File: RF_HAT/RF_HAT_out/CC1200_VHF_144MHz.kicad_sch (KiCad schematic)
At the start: 42 parts, among them J2 SMA, U2 CC1200RHBR, Y2 40MHz

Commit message: switch to SMD pico
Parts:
- TP5, TP6, TP7, TP8: value (none) -> ~

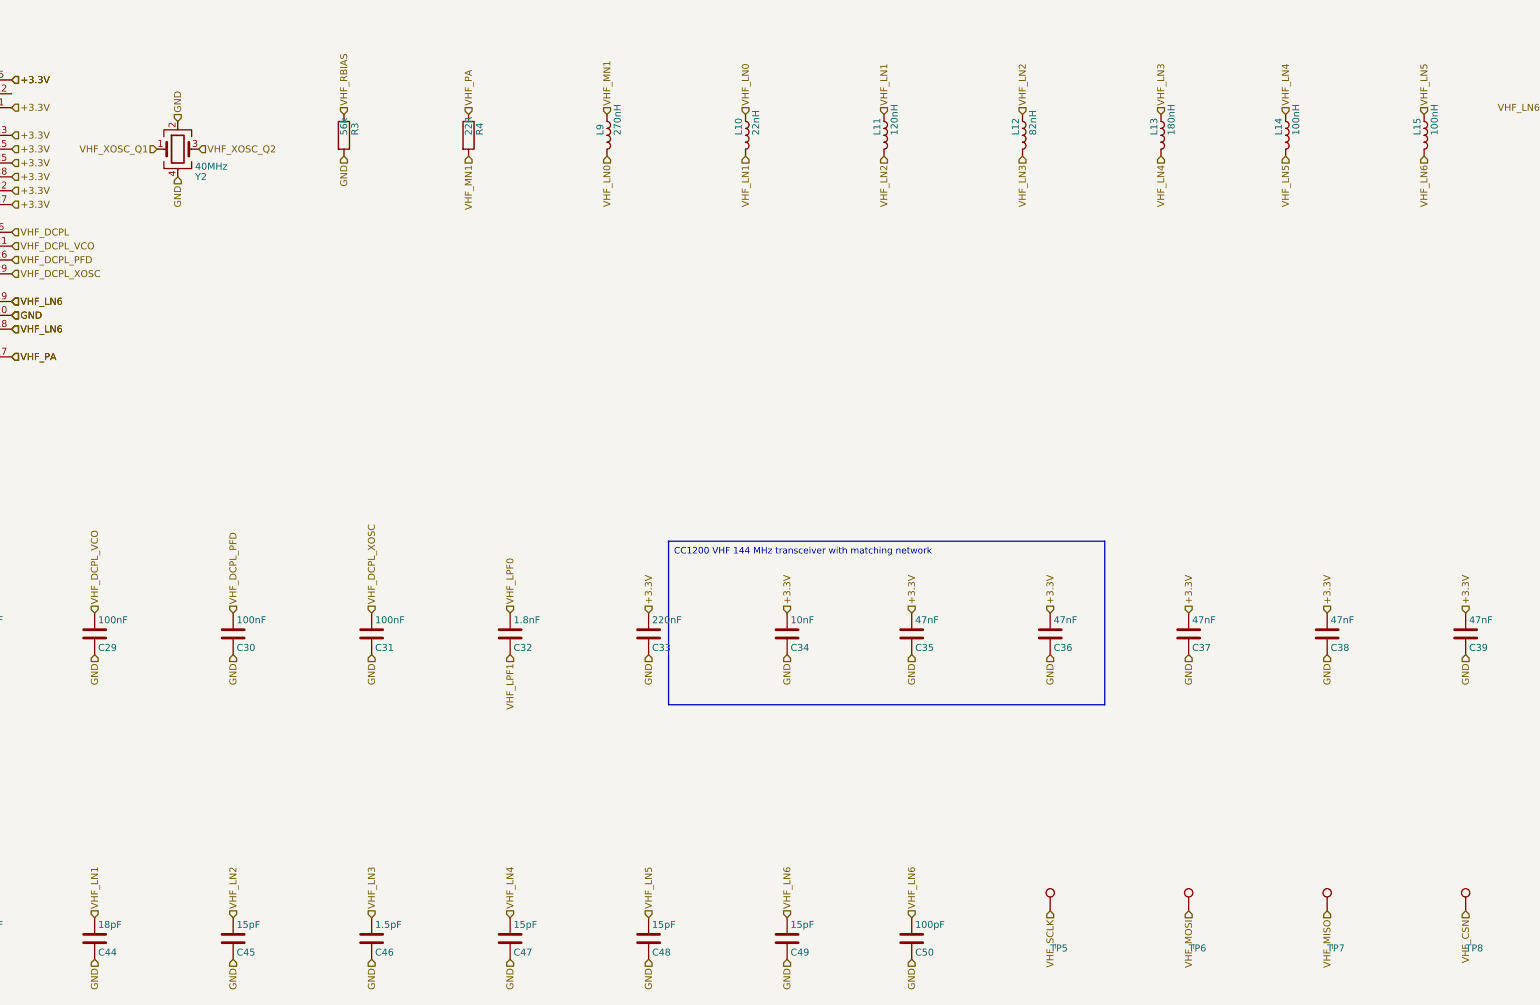
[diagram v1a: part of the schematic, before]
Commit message: switched to 0603 for all passives
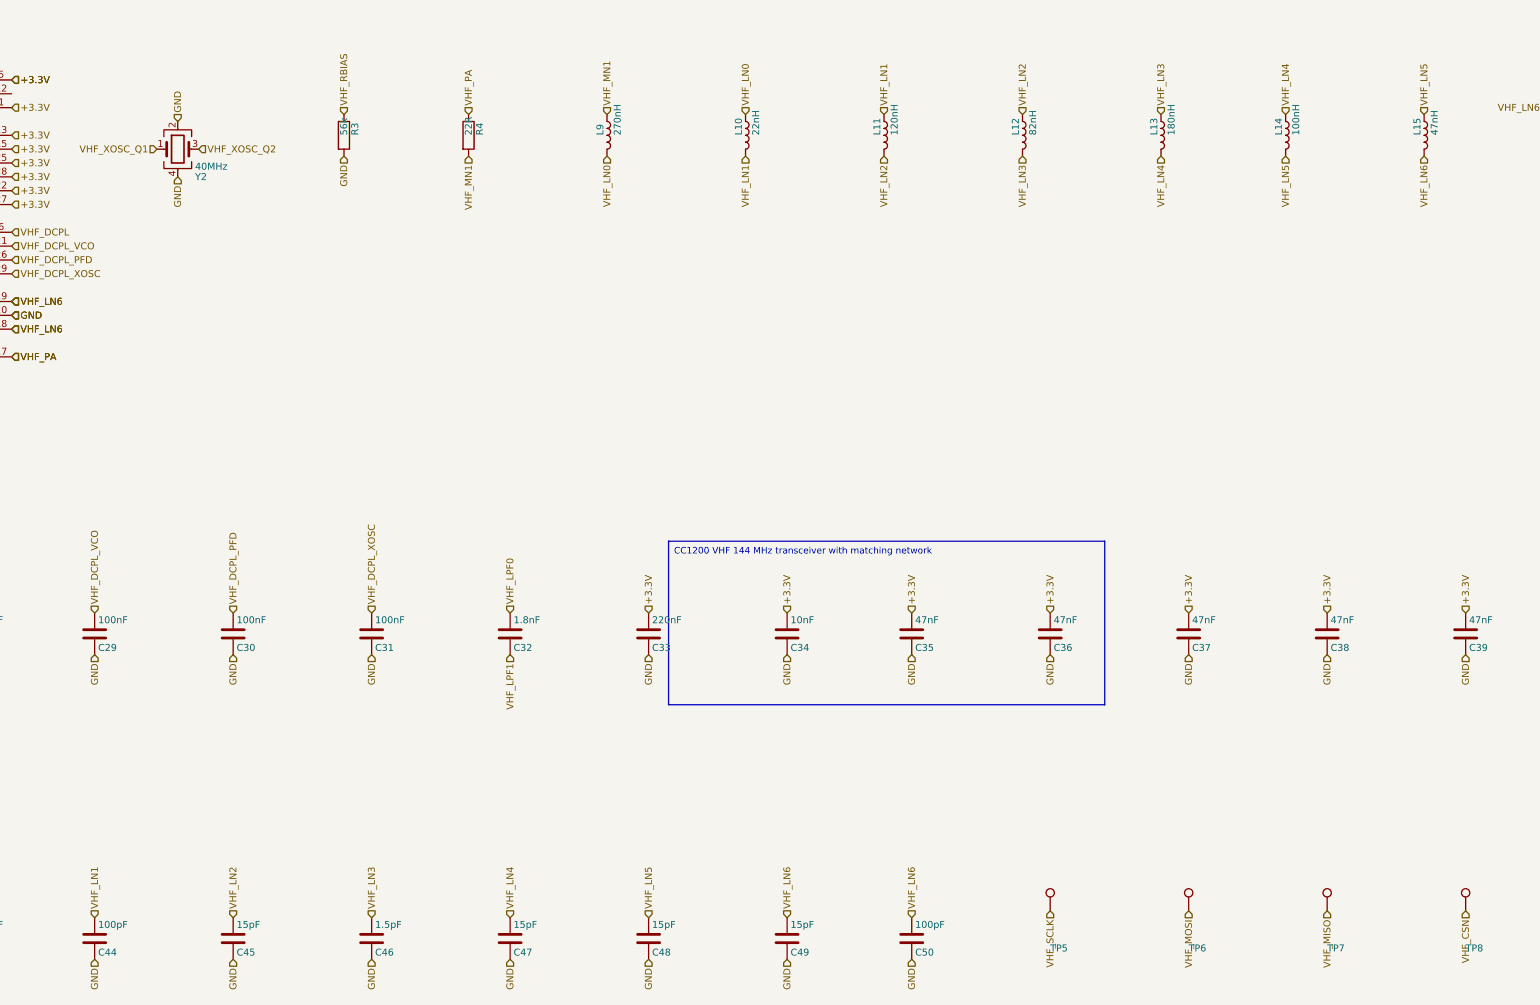
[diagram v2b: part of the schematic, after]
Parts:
- C26, C27: footprint Capacitor_SMD:C_0805_2012Metric -> Capacitor_SMD:C_0603_1608Metric; hierarchy_path /03cc9bb1-75ec-4755-9977-259c49401791/b9885f1a-c8d9-48d7-b8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 -> /bd07fb41-9ea7-4d0f-b403-cbcdc979b1cd/be5c3a7c-20a8-4363-bf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; root_uuid 03cc9bb1-75ec-4755-9977-259c49401791 -> bd07fb41-9ea7-4d0f-b403-cbcdc979b1cd
- C28, C29, C30, C31, C32, C33, C34, C35, C36, C37, C38, C39, C40, C41, C42: footprint Capacitor_SMD:C_0402_1005Metric -> Capacitor_SMD:C_0603_1608Metric; hierarchy_path /03cc9bb1-75ec-4755-9977-259c49401791/b9885f1a-c8d9-48d7-b8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 -> /bd07fb41-9ea7-4d0f-b403-cbcdc979b1cd/be5c3a7c-20a8-4363-bf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; root_uuid 03cc9bb1-75ec-4755-9977-259c49401791 -> bd07fb41-9ea7-4d0f-b403-cbcdc979b1cd
- C43, C45, C46, C47, C48, C49, C50, J2, L10, L11, L12, L13, L14, L9, TP5, TP6, TP7, TP8, U2, Y2: hierarchy_path /03cc9bb1-75ec-4755-9977-259c49401791/b9885f1a-c8d9-48d7-b8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 -> /bd07fb41-9ea7-4d0f-b403-cbcdc979b1cd/be5c3a7c-20a8-4363-bf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; root_uuid 03cc9bb1-75ec-4755-9977-259c49401791 -> bd07fb41-9ea7-4d0f-b403-cbcdc979b1cd
- C44: value 18pF -> 100pF; hierarchy_path /03cc9bb1-75ec-4755-9977-259c49401791/b9885f1a-c8d9-48d7-b8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 -> /bd07fb41-9ea7-4d0f-b403-cbcdc979b1cd/be5c3a7c-20a8-4363-bf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; root_uuid 03cc9bb1-75ec-4755-9977-259c49401791 -> bd07fb41-9ea7-4d0f-b403-cbcdc979b1cd
- FB2: footprint Inductor_SMD:L_0402_1005Metric -> Inductor_SMD:L_0603_1608Metric; hierarchy_path /03cc9bb1-75ec-4755-9977-259c49401791/b9885f1a-c8d9-48d7-b8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 -> /bd07fb41-9ea7-4d0f-b403-cbcdc979b1cd/be5c3a7c-20a8-4363-bf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; root_uuid 03cc9bb1-75ec-4755-9977-259c49401791 -> bd07fb41-9ea7-4d0f-b403-cbcdc979b1cd
- L15: value 100nH -> 47nH; hierarchy_path /03cc9bb1-75ec-4755-9977-259c49401791/b9885f1a-c8d9-48d7-b8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 -> /bd07fb41-9ea7-4d0f-b403-cbcdc979b1cd/be5c3a7c-20a8-4363-bf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; root_uuid 03cc9bb1-75ec-4755-9977-259c49401791 -> bd07fb41-9ea7-4d0f-b403-cbcdc979b1cd
- R3: footprint Resistor_SMD:R_0402_1005Metric -> Resistor_SMD:R_0603_1608Metric; hierarchy_path /03cc9bb1-75ec-4755-9977-259c49401791/b9885f1a-c8d9-48d7-b8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 -> /bd07fb41-9ea7-4d0f-b403-cbcdc979b1cd/be5c3a7c-20a8-4363-bf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; root_uuid 03cc9bb1-75ec-4755-9977-259c49401791 -> bd07fb41-9ea7-4d0f-b403-cbcdc979b1cd
- R4: footprint Resistor_SMD:R_0805_2012Metric -> Resistor_SMD:R_0603_1608Metric; hierarchy_path /03cc9bb1-75ec-4755-9977-259c49401791/b9885f1a-c8d9-48d7-b8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 -> /bd07fb41-9ea7-4d0f-b403-cbcdc979b1cd/be5c3a7c-20a8-4363-bf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; root_uuid 03cc9bb1-75ec-4755-9977-259c49401791 -> bd07fb41-9ea7-4d0f-b403-cbcdc979b1cd

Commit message: first routing of signals
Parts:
- removed TP5, TP6, TP7, TP8: ~, TestPoint:TestPoint_Pad_D1.0mm, symbol Connector:TestPoint
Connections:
- net +3.3V: no longer C33.1, C34.1, C35.1, C36.1, C37.1, C38.1, C39.1, C40.1, C41.1, U2.1 (VDD_GUARD), U2.13 (AVDD_IF), U2.15 (AVDD_RF), U2.22 (AVDD_SYNTH1), U2.25 (AVDD_PFD_CHP), U2.27 (AVDD_SYNTH2), U2.28 (AVDD_XOSC), U2.5 (DVDD)
- net VHF_AVDD_FILT: now also C33.1, C34.1, C35.1, C36.1, C37.1, C38.1, C39.1, C40.1, C41.1, U2.1 (VDD_GUARD), U2.12 (DVDD), U2.13 (AVDD_IF), U2.15 (AVDD_RF), U2.22 (AVDD_SYNTH1), U2.25 (AVDD_PFD_CHP), U2.27 (AVDD_SYNTH2), U2.28 (AVDD_XOSC), U2.5 (DVDD)

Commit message: Restructured kicad schematic for CC1200 PI_HAT readablitity based on M17 reference schematics
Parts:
- removed C48, C49: 15pF, Capacitor_SMD:C_0603_1608Metric, symbol Device:C
- removed C50: 100pF, Capacitor_SMD:C_0603_1608Metric, symbol Device:C
- removed FB2: 1k@100MHz, Inductor_SMD:L_0603_1608Metric, symbol Device:FerriteBead
- removed R4: 22R, Resistor_SMD:R_0603_1608Metric, symbol Device:R
- added C11, C20: 15pF, Capacitor_SMD:C_0603_1608Metric, symbol Device:C
- added C23: 1.8nF, Capacitor_SMD:C_0603_1608Metric, symbol Device:C
- added C25: 47nF, Capacitor_SMD:C_0603_1608Metric, symbol Device:C
- added L16: 82nH, Inductor_SMD:L_0603_1608Metric, symbol Device:L
- added R1, R2: 10k, Resistor_SMD:R_0603_1608Metric, symbol Device:R
- added R8: 22R, Resistor_SMD:R_0603_1608Metric, symbol Device:R
- C26: value 15pF -> 47nF; hierarchy_path /bd07fb41-9ea7-4d0f-b403-cbcdc979b1cd/be5c3a7c-20a8-4363-bf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 -> /300cf3d4-e317-44c8-acd8-5f9989779c7c/4304a2bc-ba15-4549-9a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; root_uuid bd07fb41-9ea7-4d0f-b403-cbcdc979b1cd -> 300cf3d4-e317-44c8-acd8-5f9989779c7c
- C27, C35, C36, C37, C40, C43, C45, J2, R3, U2, Y2: hierarchy_path /bd07fb41-9ea7-4d0f-b403-cbcdc979b1cd/be5c3a7c-20a8-4363-bf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 -> /300cf3d4-e317-44c8-acd8-5f9989779c7c/4304a2bc-ba15-4549-9a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; root_uuid bd07fb41-9ea7-4d0f-b403-cbcdc979b1cd -> 300cf3d4-e317-44c8-acd8-5f9989779c7c
- C28, C29, C30: value 100nF -> 47nF; hierarchy_path /bd07fb41-9ea7-4d0f-b403-cbcdc979b1cd/be5c3a7c-20a8-4363-bf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 -> /300cf3d4-e317-44c8-acd8-5f9989779c7c/4304a2bc-ba15-4549-9a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; root_uuid bd07fb41-9ea7-4d0f-b403-cbcdc979b1cd -> 300cf3d4-e317-44c8-acd8-5f9989779c7c
- C31: value 100nF -> 10nF; hierarchy_path /bd07fb41-9ea7-4d0f-b403-cbcdc979b1cd/be5c3a7c-20a8-4363-bf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 -> /300cf3d4-e317-44c8-acd8-5f9989779c7c/4304a2bc-ba15-4549-9a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; root_uuid bd07fb41-9ea7-4d0f-b403-cbcdc979b1cd -> 300cf3d4-e317-44c8-acd8-5f9989779c7c
- C32: value 1.8nF -> 15pF; hierarchy_path /bd07fb41-9ea7-4d0f-b403-cbcdc979b1cd/be5c3a7c-20a8-4363-bf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 -> /300cf3d4-e317-44c8-acd8-5f9989779c7c/4304a2bc-ba15-4549-9a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; root_uuid bd07fb41-9ea7-4d0f-b403-cbcdc979b1cd -> 300cf3d4-e317-44c8-acd8-5f9989779c7c
- C33: value 220nF -> 47nF; hierarchy_path /bd07fb41-9ea7-4d0f-b403-cbcdc979b1cd/be5c3a7c-20a8-4363-bf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 -> /300cf3d4-e317-44c8-acd8-5f9989779c7c/4304a2bc-ba15-4549-9a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; root_uuid bd07fb41-9ea7-4d0f-b403-cbcdc979b1cd -> 300cf3d4-e317-44c8-acd8-5f9989779c7c
- C34: value 10nF -> 220nF; hierarchy_path /bd07fb41-9ea7-4d0f-b403-cbcdc979b1cd/be5c3a7c-20a8-4363-bf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 -> /300cf3d4-e317-44c8-acd8-5f9989779c7c/4304a2bc-ba15-4549-9a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; root_uuid bd07fb41-9ea7-4d0f-b403-cbcdc979b1cd -> 300cf3d4-e317-44c8-acd8-5f9989779c7c
- C38, C39: value 47nF -> 100pF; hierarchy_path /bd07fb41-9ea7-4d0f-b403-cbcdc979b1cd/be5c3a7c-20a8-4363-bf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 -> /300cf3d4-e317-44c8-acd8-5f9989779c7c/4304a2bc-ba15-4549-9a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; root_uuid bd07fb41-9ea7-4d0f-b403-cbcdc979b1cd -> 300cf3d4-e317-44c8-acd8-5f9989779c7c
- C41: value 47nF -> 10nF; hierarchy_path /bd07fb41-9ea7-4d0f-b403-cbcdc979b1cd/be5c3a7c-20a8-4363-bf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 -> /300cf3d4-e317-44c8-acd8-5f9989779c7c/4304a2bc-ba15-4549-9a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; root_uuid bd07fb41-9ea7-4d0f-b403-cbcdc979b1cd -> 300cf3d4-e317-44c8-acd8-5f9989779c7c
- C42: value 10nF -> 47nF; hierarchy_path /bd07fb41-9ea7-4d0f-b403-cbcdc979b1cd/be5c3a7c-20a8-4363-bf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 -> /300cf3d4-e317-44c8-acd8-5f9989779c7c/4304a2bc-ba15-4549-9a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; root_uuid bd07fb41-9ea7-4d0f-b403-cbcdc979b1cd -> 300cf3d4-e317-44c8-acd8-5f9989779c7c
- C44: value 100pF -> 1.5pF; hierarchy_path /bd07fb41-9ea7-4d0f-b403-cbcdc979b1cd/be5c3a7c-20a8-4363-bf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 -> /300cf3d4-e317-44c8-acd8-5f9989779c7c/4304a2bc-ba15-4549-9a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; root_uuid bd07fb41-9ea7-4d0f-b403-cbcdc979b1cd -> 300cf3d4-e317-44c8-acd8-5f9989779c7c
- C46: value 1.5pF -> 15pF; hierarchy_path /bd07fb41-9ea7-4d0f-b403-cbcdc979b1cd/be5c3a7c-20a8-4363-bf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 -> /300cf3d4-e317-44c8-acd8-5f9989779c7c/4304a2bc-ba15-4549-9a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; root_uuid bd07fb41-9ea7-4d0f-b403-cbcdc979b1cd -> 300cf3d4-e317-44c8-acd8-5f9989779c7c
- C47: value 15pF -> 100pF; hierarchy_path /bd07fb41-9ea7-4d0f-b403-cbcdc979b1cd/be5c3a7c-20a8-4363-bf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 -> /300cf3d4-e317-44c8-acd8-5f9989779c7c/4304a2bc-ba15-4549-9a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; root_uuid bd07fb41-9ea7-4d0f-b403-cbcdc979b1cd -> 300cf3d4-e317-44c8-acd8-5f9989779c7c
- L10: value 22nH -> 100nH; hierarchy_path /bd07fb41-9ea7-4d0f-b403-cbcdc979b1cd/be5c3a7c-20a8-4363-bf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 -> /300cf3d4-e317-44c8-acd8-5f9989779c7c/4304a2bc-ba15-4549-9a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; root_uuid bd07fb41-9ea7-4d0f-b403-cbcdc979b1cd -> 300cf3d4-e317-44c8-acd8-5f9989779c7c
- L11: value 120nH -> 47nH; hierarchy_path /bd07fb41-9ea7-4d0f-b403-cbcdc979b1cd/be5c3a7c-20a8-4363-bf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 -> /300cf3d4-e317-44c8-acd8-5f9989779c7c/4304a2bc-ba15-4549-9a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; root_uuid bd07fb41-9ea7-4d0f-b403-cbcdc979b1cd -> 300cf3d4-e317-44c8-acd8-5f9989779c7c
- L12: value 82nH -> 100nH; hierarchy_path /bd07fb41-9ea7-4d0f-b403-cbcdc979b1cd/be5c3a7c-20a8-4363-bf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 -> /300cf3d4-e317-44c8-acd8-5f9989779c7c/4304a2bc-ba15-4549-9a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; root_uuid bd07fb41-9ea7-4d0f-b403-cbcdc979b1cd -> 300cf3d4-e317-44c8-acd8-5f9989779c7c
- L13: value 180nH -> 270nH; hierarchy_path /bd07fb41-9ea7-4d0f-b403-cbcdc979b1cd/be5c3a7c-20a8-4363-bf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 -> /300cf3d4-e317-44c8-acd8-5f9989779c7c/4304a2bc-ba15-4549-9a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; root_uuid bd07fb41-9ea7-4d0f-b403-cbcdc979b1cd -> 300cf3d4-e317-44c8-acd8-5f9989779c7c
- L14: value 100nH -> 22nH; hierarchy_path /bd07fb41-9ea7-4d0f-b403-cbcdc979b1cd/be5c3a7c-20a8-4363-bf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 -> /300cf3d4-e317-44c8-acd8-5f9989779c7c/4304a2bc-ba15-4549-9a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; root_uuid bd07fb41-9ea7-4d0f-b403-cbcdc979b1cd -> 300cf3d4-e317-44c8-acd8-5f9989779c7c
- L15: value 47nH -> 120nH; hierarchy_path /bd07fb41-9ea7-4d0f-b403-cbcdc979b1cd/be5c3a7c-20a8-4363-bf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 -> /300cf3d4-e317-44c8-acd8-5f9989779c7c/4304a2bc-ba15-4549-9a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; root_uuid bd07fb41-9ea7-4d0f-b403-cbcdc979b1cd -> 300cf3d4-e317-44c8-acd8-5f9989779c7c
- L9: value 270nH -> 100nH; hierarchy_path /bd07fb41-9ea7-4d0f-b403-cbcdc979b1cd/be5c3a7c-20a8-4363-bf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 -> /300cf3d4-e317-44c8-acd8-5f9989779c7c/4304a2bc-ba15-4549-9a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; root_uuid bd07fb41-9ea7-4d0f-b403-cbcdc979b1cd -> 300cf3d4-e317-44c8-acd8-5f9989779c7c
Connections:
- net GND: now also C32.2, L9.2, R3.1, C11.2, C20.2, C25.2; no longer C27.2, C38.2, C39.2, C44.2, C45.2, C47.2, R3.2, U2.20 (LNA_N)
- net VHF_AVDD_FILT renamed +3V3
- net +3V3: now also C26.1, C29.1, C30.1, C43.1, R1.1, R2.1, R8.1; no longer C34.1, C39.1
- net VHF_CSN renamed UHF_CSN
- net UHF_CSN: now also R1.2
- net VHF_DCPL: no longer names the net of C28.1
- net VHF_DCPL: now also U2.26 (DCPL_PFD_CHP); no longer U2.6 (DCPL)
- removed net VHF_DCPL_PFD: C30.1, U2.26 (DCPL_PFD_CHP)
- net VHF_DCPL_VCO: no longer names the net of U2.21 (DCPL_VCO)
- net VHF_DCPL_VCO: now also C31.1; no longer C29.1
- net VHF_DCPL_XOSC: no longer names the net of U2.29 (DCPL_XOSC)
- net VHF_DCPL_XOSC: now also C25.1; no longer C31.1
- net VHF_GPIO0 renamed UHF_GPIO0
- net VHF_GPIO2 renamed UHF_GPIO2
- net VHF_GPIO3 renamed UHF_GPIO3
- removed net VHF_LN0: C43.1, L10.1, L9.2
- removed net VHF_LN1: C44.1, L10.2, L11.1
- removed net VHF_LN2: C45.1, L11.2, L12.1
- removed net VHF_LN3: C46.1, L12.2, L13.1
- removed net VHF_LN4: C47.1, L13.2, L14.1
- net VHF_LN5: no longer names the net of L14.2, L15.1
- net VHF_LN5: now also C44.2, C45.1
- removed net VHF_LN6: J2.1 (In), L15.2, U2.18 (TRX_SW), U2.19 (LNA_P)
- net VHF_LPF0: no longer names the net of C32.1
- net VHF_LPF0: now also L10.2, L12.1, U2.20 (LNA_N); no longer U2.23 (LPF0)
- net VHF_LPF1: no longer names the net of U2.24 (LPF1)
- net VHF_LPF1: now also C23.1; no longer C32.2
- net VHF_MISO renamed UHF_MISO
- net VHF_MN1: no longer names the net of L9.1
- net VHF_MN1: now also C27.1, L10.1, U2.19 (LNA_P)
- net VHF_MOSI renamed UHF_MOSI
- net VHF_PA: no longer names the net of U2.17 (PA)
- net VHF_PA: now also C39.1, L13.2
- net VHF_RBIAS: no longer names the net of U2.14 (RBIAS)
- net VHF_RBIAS: now also R3.2; no longer R3.1
- net VHF_RESET renamed UHF_RESET
- net UHF_RESET: now also R2.2
- net VHF_SCLK renamed UHF_SCLK
- net VHF_XOSC_Q1: no longer names the net of U2.30 (XOSC_Q1), Y2.1
- net VHF_XOSC_Q1: now also C11.1; no longer C26.1
- net VHF_XOSC_Q2: no longer names the net of U2.31 (XOSC_Q2), Y2.3
- net VHF_XOSC_Q2: now also C20.1; no longer C27.1
- new net: C47.2, J2.1 (In)
- new net: C38.2, L13.1, R8.2
- new net: C45.2, L11.2, U2.18 (TRX_SW)
- new net: C47.1, L16.2
- new net: C39.2, C44.1, L14.1
- new net: C34.1, U2.6 (DCPL)
- new net: C23.2, U2.23 (LPF0)
- new net: C27.2, L11.1, L12.2
- new net: C46.1, L15.2, L16.1
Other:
- note added: "CC1200 VHF 144 MHz Matching Network Source: TI CC1120EM 169 MHz ref design (TIDR220/TIDR222) Scaled from 169 MHz to 144 MHz band. No official TI reference exists for CC1200 at 136-160 MHz. WARNING: VHF values are starting points only. VNA tuning required during board bring-up. Topology identical to UHF (3-path, shared SMA): TX: PA → C2-L1-C1-L2-C3-L3-C4 → C10(DC block) → SMA TRX: TRX_SW → C3 to T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"

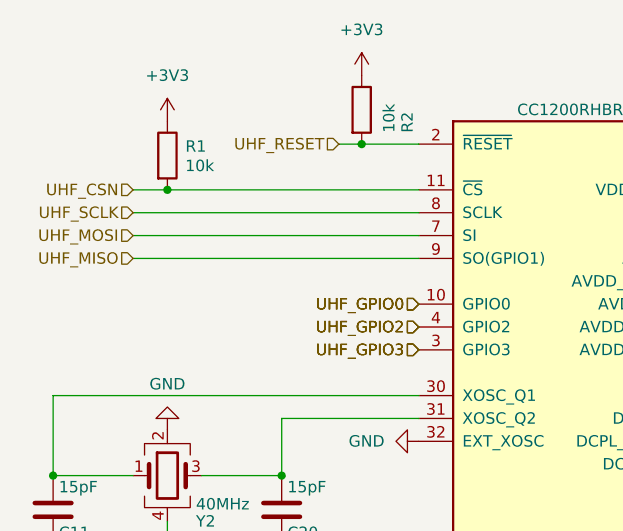
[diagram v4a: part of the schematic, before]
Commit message: fixed schematic and updated readme's
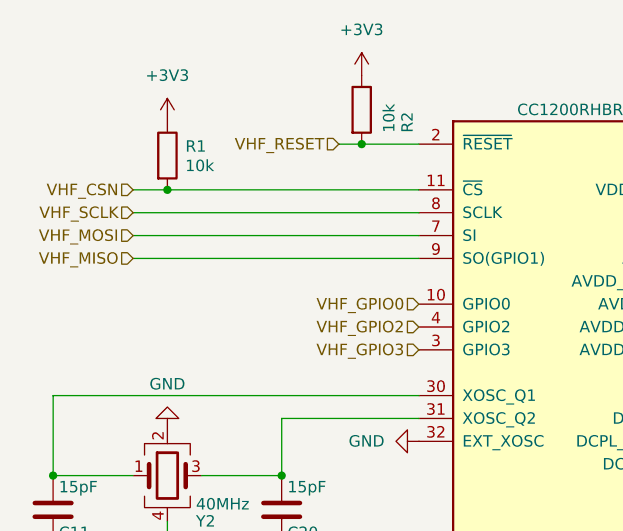
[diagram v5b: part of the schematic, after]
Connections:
- net UHF_CSN renamed VHF_CSN
- net UHF_GPIO0 renamed VHF_GPIO0
- net UHF_GPIO2 renamed VHF_GPIO2
- net UHF_GPIO3 renamed VHF_GPIO3
- net UHF_MISO renamed VHF_MISO
- net UHF_MOSI renamed VHF_MOSI
- net UHF_RESET renamed VHF_RESET
- net UHF_SCLK renamed VHF_SCLK
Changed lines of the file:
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@@
 		)
 	)
-	(hierarchical_label "UHF_RESET"
+	(hierarchical_label "VHF_RESET"
 		(shape input)
 		(at 71.12 48.26 180)
@@
 		)
 	)
-	(hierarchical_label "UHF_GPIO2"
+	(hierarchical_label "VHF_MOSI"
+		(shape input)
+		(at 48.26 58.42 180)
+		(effects
+			(font
+				(size 1.27 1.27)
+			)
+			(justify right)
+		)
+	)
+	(hierarchical_label "VHF_SCLK"
+		(shape input)
+		(at 48.26 55.88 180)
+		(effects
+			(font
+				(size 1.27 1.27)
+			)
+			(justify right)
+		)
+	)
+	(hierarchical_label "VHF_CSN"
+		(shape input)
+		(at 48.26 53.34 180)
+		(effects
+			(font
+				(size 1.27 1.27)
+			)
+			(justify right)
+		)
+	)
+	(hierarchical_label "VHF_GPIO0"
+		(shape input)
+		(at 80.01 66.04 180)
+		(effects
+			(font
+				(size 1.27 1.27)
+			)
+			(justify right)
+		)
+	)
+	(hierarchical_label "VHF_GPIO3"
+		(shape input)
+		(at 80.01 71.12 180)
+		(effects
+			(font
+				(size 1.27 1.27)
+			)
+			(justify right)
+		)
+	)
+	(hierarchical_label "VHF_GPIO2"
 		(shape input)
 		(at 80.01 68.58 180)
@@
 		)
 	)
-	(hierarchical_label "UHF_MOSI"
-		(shape input)
-		(at 48.26 58.42 180)
-		(effects
-			(font
-				(size 1.27 1.27)
-			)
-			(justify right)
-		)
-	)
-	(hierarchical_label "UHF_GPIO0"
-		(shape input)
-		(at 80.01 66.04 180)
-		(effects
-			(font
-				(size 1.27 1.27)
-			)
-			(justify right)
-		)
-	)
-	(hierarchical_label "UHF_SCLK"
-		(shape input)
-		(at 48.26 55.88 180)
-		(effects
-			(font
-				(size 1.27 1.27)
-			)
-			(justify right)
-		)
-	)
-	(hierarchical_label "UHF_CSN"
-		(shape input)
-		(at 48.26 53.34 180)
-		(effects
-			(font
-				(size 1.27 1.27)
-			)
-			(justify right)
-		)
-	)
-	(hierarchical_label "UHF_GPIO0"
-		(shape input)
-		(at 80.01 66.04 180)
-		(effects
-			(font
-				(size 1.27 1.27)
-			)
-			(justify right)
-		)
-	)
-	(hierarchical_label "UHF_GPIO3"
-		(shape input)
-		(at 80.01 71.12 180)
-		(effects
-			(font
-				(size 1.27 1.27)
-			)
-			(justify right)
-		)
-	)
-	(hierarchical_label "UHF_GPIO3"
-		(shape input)
-		(at 80.01 71.12 180)
-		(effects
-			(font
-				(size 1.27 1.27)
-			)
-			(justify right)
-		)
-	)
-	(hierarchical_label "UHF_GPIO2"
-		(shape input)
-		(at 80.01 68.58 180)
-		(effects
-			(font
-				(size 1.27 1.27)
-			)
-			(justify right)
-		)
-	)
-	(hierarchical_label "UHF_MISO"
+	(hierarchical_label "VHF_MISO"
 		(shape input)
 		(at 48.26 60.96 180)

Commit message: did final routing and added Farnell and LCSC numbers to all components
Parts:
- C11, C20, C27, C32, C45, C46: Farnell (none) -> 721980; LCSC (none) -> C1644
- C23: Farnell (none) -> 1813422; LCSC (none) -> C343008
- C25, C26, C28, C29, C30, C33, C35, C36, C37, C40, C42: Farnell (none) -> 2495363; LCSC (none) -> C1622
- C31, C41: Farnell (none) -> 1759022; LCSC (none) -> C57112
- C34: Farnell (none) -> 1828900; LCSC (none) -> C21120
- C38, C39, C43, C47: Farnell (none) -> 722080; LCSC (none) -> C14858
- C44: Farnell (none) -> 721864; LCSC (none) -> C695130
- J2: Farnell (none) -> 2112467
- L10, L12, L9: Farnell (none) -> 9528032; LCSC (none) -> C98089
- L11: Farnell (none) -> 1515390; LCSC (none) -> C29683
- L13: Farnell (none) -> 3471564; LCSC (none) -> C668477
- L14: Farnell (none) -> 1515382; LCSC (none) -> C98071
- L15: Farnell (none) -> 3678407; LCSC (none) -> C307612
- L16: Farnell (none) -> 1515396; LCSC (none) -> C98085
- R1, R2: Farnell (none) -> 9238603; LCSC (none) -> C25804
- R3: Farnell (none) -> 9238697; LCSC (none) -> C23206
- R8: Farnell (none) -> 9238280; LCSC (none) -> C23345
- U2: Farnell (none) -> 2345430; LCSC (none) -> C122881
- Y2: Farnell (none) -> 1712847; LCSC (none) -> C5380316
